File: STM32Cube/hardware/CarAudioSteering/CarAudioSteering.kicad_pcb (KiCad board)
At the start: 4 copper layers, 49.5 x 21.6 mm, 27 parts, among them J1 UART, J2 SWD, J3 Remote, J4 Buttons, Q1 AO3400A, U1 STM32F030F4Px, U2 AD5272BRM, Y1 Crystal

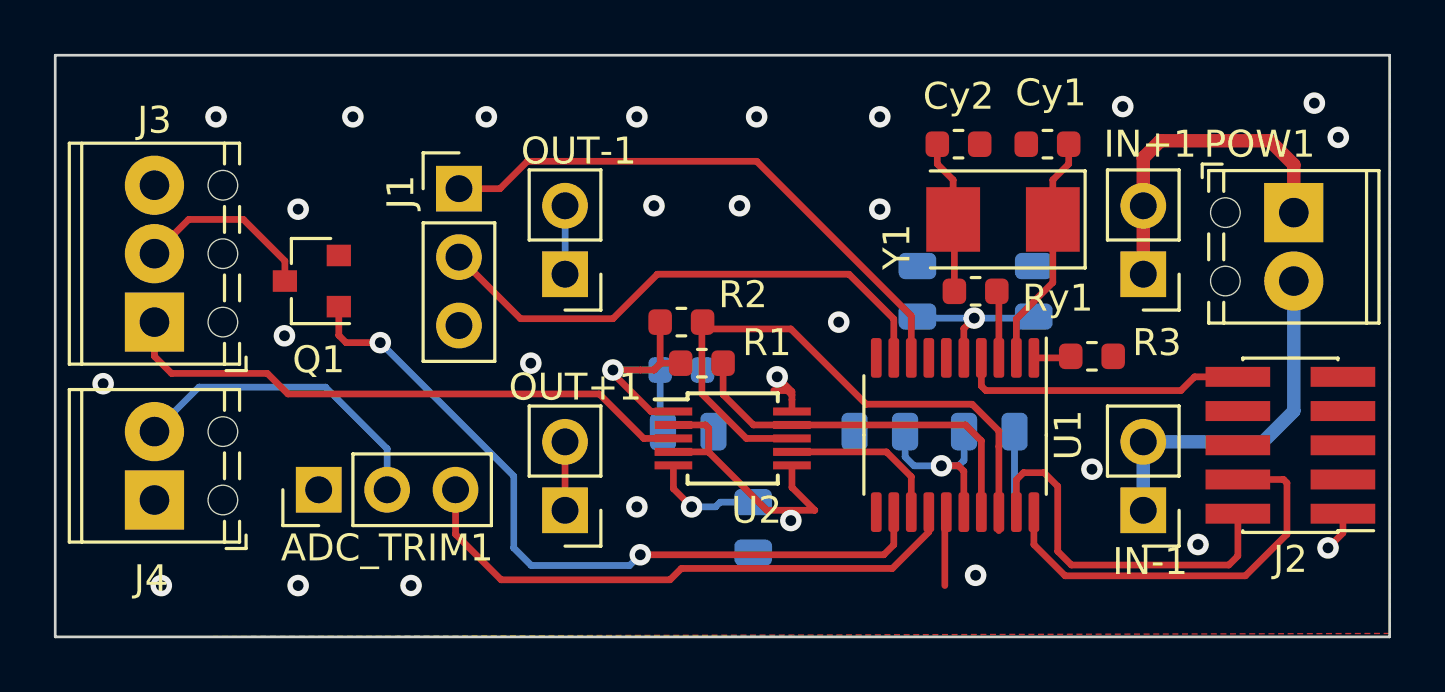
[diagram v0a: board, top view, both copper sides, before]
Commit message: Update PCB to add a MOSFET switch on the digipot output
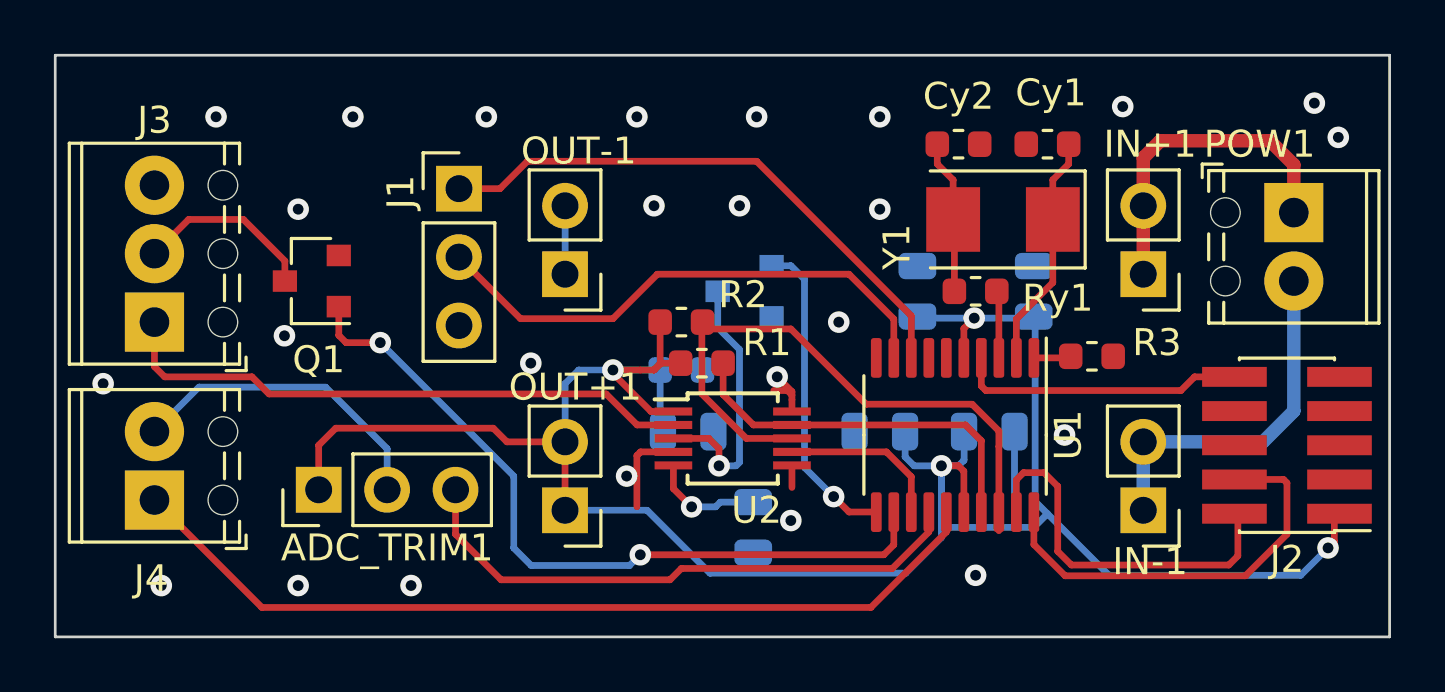
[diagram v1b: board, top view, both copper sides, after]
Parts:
- added Q2: AO3400A, Package_TO_SOT_SMD:SOT-23, B.Cu at (76.4, 72.3)
- moved J2 0.13 mm to (96.5, 78.0)
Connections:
- U1 pad 11: Net-(U1-Pad11) -> TIP_SW
- U2 pad 2: GND -> REM_TIP
- U2 pad 3: REM_TIP -> POT_W
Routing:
- net +3.3VA: track 29.2 -> 88.3 mm
- net GND: track 20.6 -> 44.8 mm, vias 26 -> 25
- net TIP_SW: track 0.00 -> 11.8 mm, vias 0 -> 1
- net POT_W: track 0.00 -> 9.99 mm, vias 0 -> 1
- removed copper zone on In1.Cu, net +3.3VA
- removed copper zone on In2.Cu, net GND
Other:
- copper layers 4 -> 2
